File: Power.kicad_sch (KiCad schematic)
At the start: 7 parts, among them J8 A/C, SW11 MAIN_SW, U3 LM7805_TO220, U6 LM7812_TO220

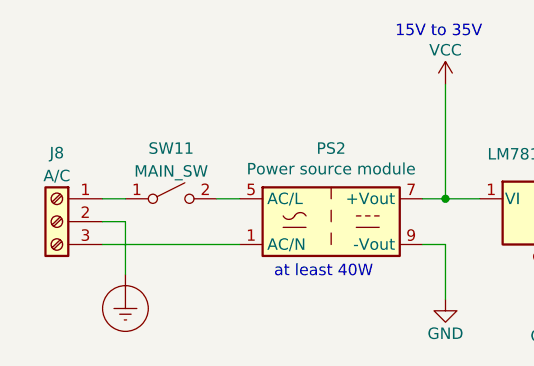
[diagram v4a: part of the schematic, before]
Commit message: Changed the power witch
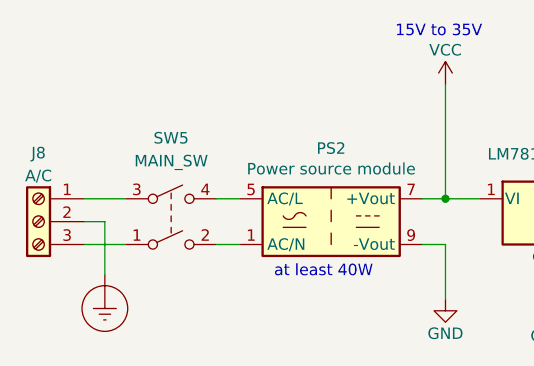
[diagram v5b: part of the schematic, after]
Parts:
- removed SW11: MAIN_SW, symbol switches:SW_SPST
- added SW5: MAIN_SW, symbol Switch:SW_DPST
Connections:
- net at J8.3 (Pin_3): now also SW5.1; no longer PS2.1 (AC/N)
- net at PS2.5 (AC/L): now also SW5.4
- net at J8.1 (Pin_1): now also SW5.3
- new net: PS2.1 (AC/N), SW5.2
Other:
- moved on the sheet: J8
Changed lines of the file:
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@@
 	(wire
 		(pts
-			(xy 102.87 95.885) (xy 118.11 95.885)
+			(xy 100.838 95.885) (xy 105.41 95.885)
 		)
 		(stroke
@@
 	(wire
 		(pts
+			(xy 115.57 95.885) (xy 118.11 95.885)
+		)
+		(stroke
+			(width 0)
+			(type default)
+		)
+	)
+	(wire
+		(pts
 			(xy 115.57 90.805) (xy 118.11 90.805)
 		)
@@
 	(wire
 		(pts
-			(xy 102.87 90.805) (xy 105.41 90.805)
-		)
-		(stroke
-			(width 0)
-			(type default)
-		)
-	)
-	(wire
-		(pts
-			(xy 105.41 93.345) (xy 102.87 93.345)
+			(xy 100.838 90.805) (xy 105.41 90.805)
+		)
+		(stroke
+			(width 0)
+			(type default)
+		)
+	)
+	(wire
+		(pts
+			(xy 103.124 93.345) (xy 100.838 93.345)
 		)
 		(stroke
@@
 	(wire
 		(pts
-			(xy 105.41 93.345) (xy 105.41 99.187)
+			(xy 103.124 93.345) (xy 103.124 99.187)
 		)
 		(stroke
@@
 	)
 	(symbol
+		(lib_id "Switch:SW_DPST")
+		(at 110.49 93.345 0)
+		(unit 1)
+		(exclude_from_sim no)
+		(in_bom yes)
+		(on_board yes)
+		(dnp no)
+		(property "Reference" "SW5"
+			(at 110.49 84.074 0)
+			(effects
+				(font
+					(size 1.27 1.27)
+				)
+			)
+		)
+		(property "Value" "MAIN_SW"
+			(at 110.49 86.614 0)
+			(effects
+				(font
+					(size 1.27 1.27)
+				)
+			)
+		)
+		(property "Footprint" ""
+			(at 110.49 93.345 0)
+			(effects
+				(font
+					(size 1.27 1.27)
+				)
+				(hide yes)
+			)
+		)
+		(property "Datasheet" "~"
+			(at 110.49 93.345 0)
+			(effects
+				(font
+					(size 1.27 1.27)
+				)
+				(hide yes)
+			)
+		)
+		(property "Description" "Double Pole Single Throw (DPST) Switch"
+			(at 110.49 93.345 0)
+			(effects
+				(font
+					(size 1.27 1.27)
+				)
+				(hide yes)
+			)
+		)
+		(pin "4"
+		)
+		(pin "3"
+		)
+		(pin "1"
+		)
+		(pin "2"
+		)
+		(instances
+			(project ""
+				(path "/443fc4b5-0df2-45f7-86a3-68fb41149ce4/5e839a07-4be5-4c9a-ad45-e94867be72dd"
+					(reference "SW5")
+					(unit 1)
+				)
+			)
+		)
+	)
+	(symbol
 		(lib_id "Converter_ACDC:HS-40024")
 		(at 128.27 93.345 0)
@@
 	)
 	(symbol
-		(lib_id "switches:SW_SPST")
-		(at 110.49 90.805 0)
-		(unit 1)
-		(exclude_from_sim no)
-		(in_bom yes)
-		(on_board yes)
-		(dnp no)
-		(fields_autoplaced yes)
-		(property "Reference" "SW11"
-			(at 110.49 85.217 0)
-			(effects
-				(font
-					(size 1.27 1.27)
-				)
-			)
-		)
-		(property "Value" "MAIN_SW"
-			(at 110.49 87.757 0)
-			(effects
-				(font
-					(size 1.27 1.27)
-				)
-			)
-		)
-		(property "Footprint" ""
-			(at 110.49 90.805 0)
-			(effects
-				(font
-					(size 1.27 1.27)
-				)
-				(hide yes)
-			)
-		)
-		(property "Datasheet" ""
-			(at 110.49 90.805 0)
-			(effects
-				(font
-					(size 1.27 1.27)
-				)
-				(hide yes)
-			)
-		)
-		(property "Description" ""
-			(at 110.49 90.805 0)
-			(effects
-				(font
-					(size 1.27 1.27)
-				)
-				(hide yes)
-			)
-		)
-		(pin "1"
-		)
-		(pin "2"
-		)
-		(instances
-			(project "GRUB"
-				(path "/443fc4b5-0df2-45f7-86a3-68fb41149ce4/5e839a07-4be5-4c9a-ad45-e94867be72dd"
-					(reference "SW11")
-					(unit 1)
-				)
-			)
-		)
-	)
-	(symbol
 		(lib_id "Connector:Screw_Terminal_01x03")
-		(at 97.79 93.345 0)
+		(at 95.758 93.345 0)
 		(mirror y)
 		(unit 1)
@@
 		(fields_autoplaced yes)
 		(property "Reference" "J8"
-			(at 97.79 85.725 0)
+			(at 95.758 85.725 0)
 			(effects
 				(font
@@
 		)
 		(property "Value" "A/C"
-			(at 97.79 88.265 0)
+			(at 95.758 88.265 0)
 			(effects
 				(font
@@
 		)
 		(property "Footprint" ""
-			(at 97.79 93.345 0)
+			(at 95.758 93.345 0)
 			(effects
 				(font
@@
 		)
 		(property "Datasheet" "~"
-			(at 97.79 93.345 0)
+			(at 95.758 93.345 0)
 			(effects
 				(font
@@
 		)
 		(property "Description" ""
-			(at 97.79 93.345 0)
+			(at 95.758 93.345 0)
 			(effects
 				(font
@@
 	(symbol
 		(lib_id "power:Earth_Protective")
-		(at 105.41 99.187 0)
+		(at 103.124 99.187 0)
 		(unit 1)
 		(exclude_from_sim no)
@@
 		(fields_autoplaced yes)
 		(property "Reference" "#PWR010"
-			(at 111.76 105.537 0)
+			(at 109.474 105.537 0)
 			(effects
 				(font
@@
 		)
 		(property "Value" "Earth_Protective"
-			(at 116.84 102.997 0)
+			(at 114.554 102.997 0)
 			(effects
 				(font
@@
 		)
 		(property "Footprint" ""
-			(at 105.41 101.727 0)
+			(at 103.124 101.727 0)
 			(effects
 				(font
@@
 		)
 		(property "Datasheet" "~"
-			(at 105.41 101.727 0)
+			(at 103.124 101.727 0)
 			(effects
 				(font
@@
 		)
 		(property "Description" ""
-			(at 105.41 99.187 0)
-			(effects
-				(font
+			(at 103.124 99.187 0)
+			(effects
+				(font
